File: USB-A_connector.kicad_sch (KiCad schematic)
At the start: 5 parts, among them J102 USB_A, U501 STMPS2141STR

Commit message: update BOM
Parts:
- J102: now left out of the parts list
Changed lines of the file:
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@@
   )
   (symbol (lib_id "Connector:USB_A") (at 140.97 67.31 0) (mirror y) (unit 1)
-    (in_bom yes) (on_board yes) (dnp no)
+    (in_bom no) (on_board yes) (dnp no)
     (property "Reference" "J102" (at 140.97 55.88 0)
       (effects (font (size 1.27 1.27)))

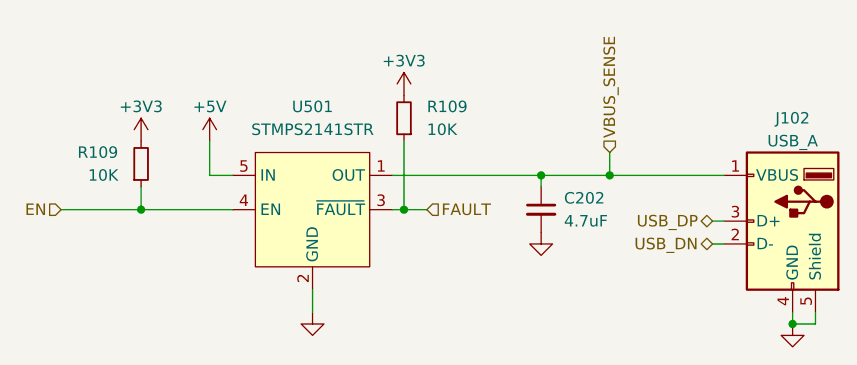
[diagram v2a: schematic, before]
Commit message: update schematic and pcb design to rev-b
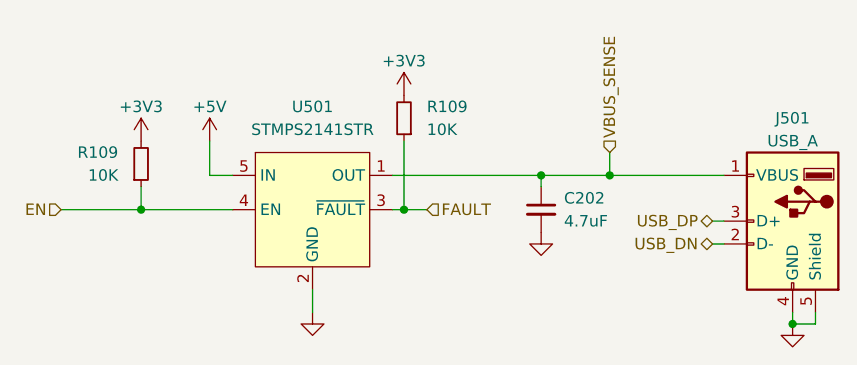
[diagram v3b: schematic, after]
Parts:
- renumbered J102 to J501

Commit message: add scoreboard connector
- add ethernet jack for scoreboard connection
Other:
- company: (none) -> Butler Electronics
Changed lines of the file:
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@@
 	(generator_version "8.0")
 	(paper "A4")
+	(title_block
+		(rev "C")
+		(company "Butler Electronics")
+		(comment 1 "Joshua Butler, MD, MHI")
+	)
 	(junction
 		(at 68.58 66.04)
